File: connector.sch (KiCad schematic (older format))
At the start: 17 parts

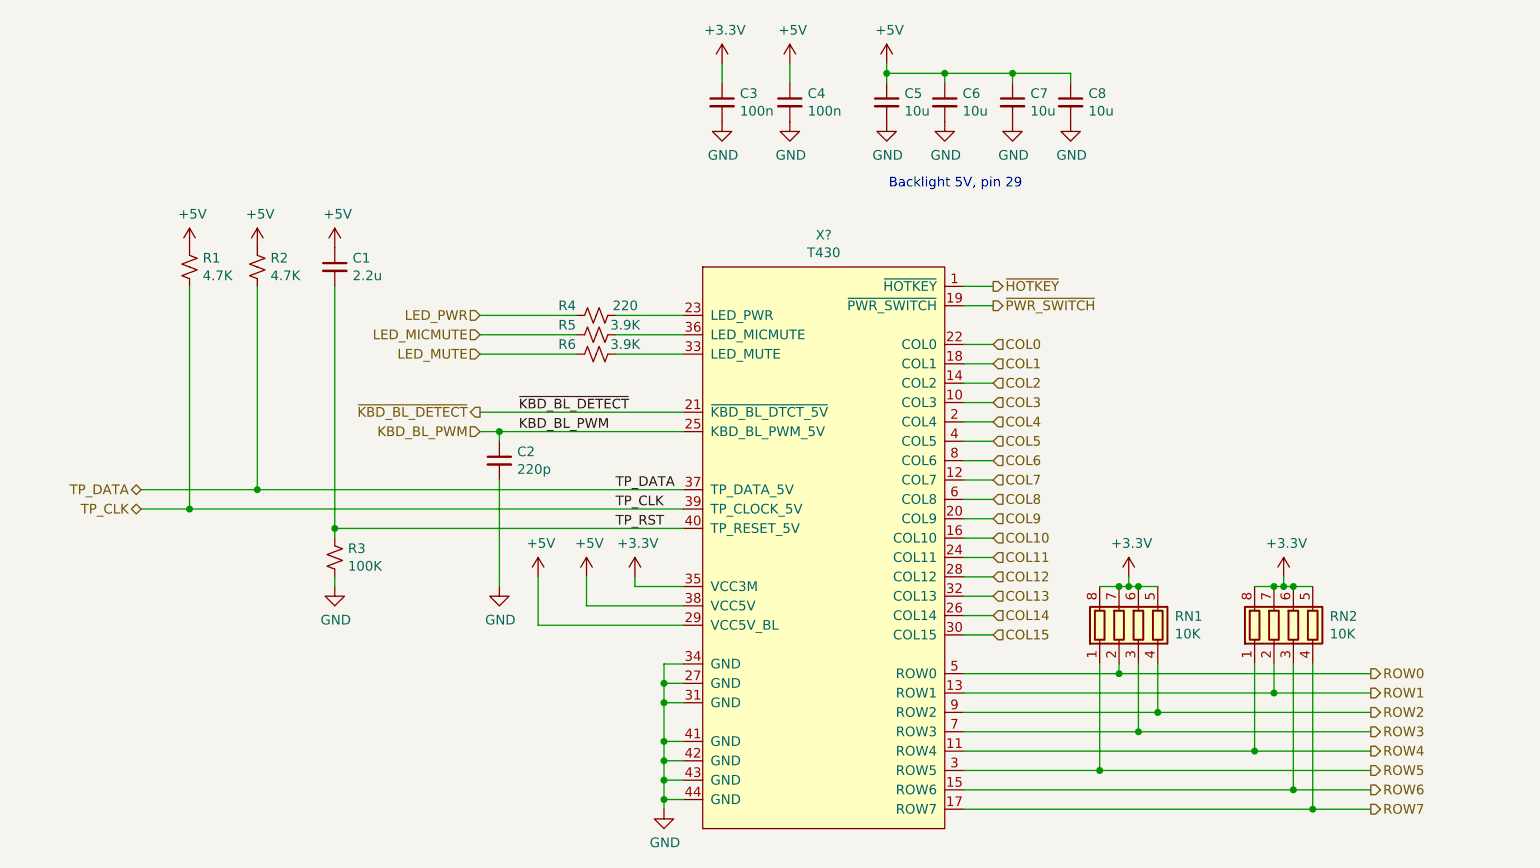
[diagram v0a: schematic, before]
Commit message: Added 'do not populate' for Trackpoint and rows
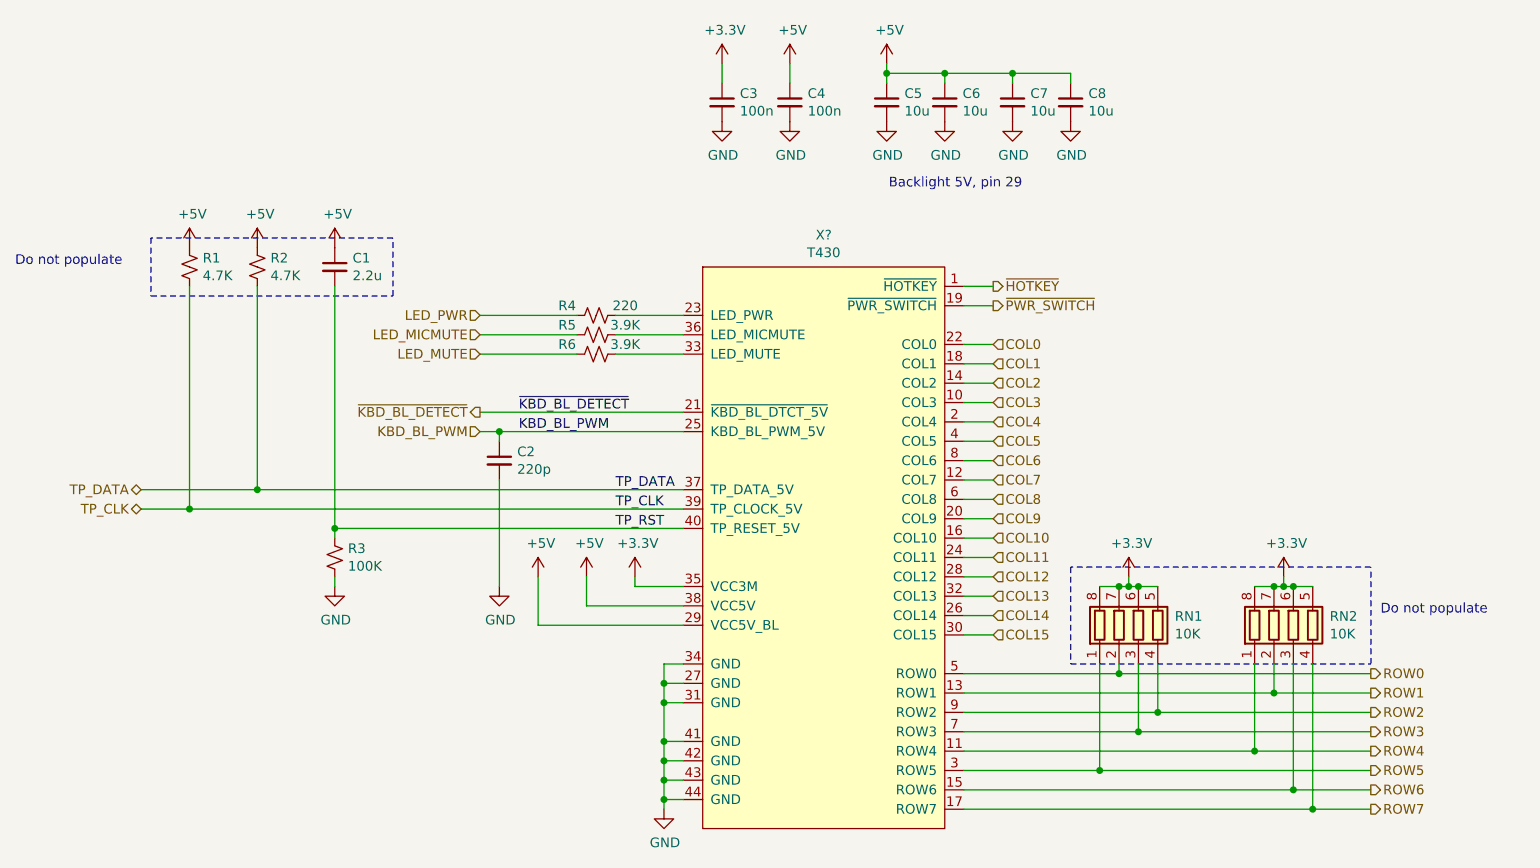
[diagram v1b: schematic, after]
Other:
- note added: "Do not populate"
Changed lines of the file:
@@
 	1    0    0    -1
 $EndComp
+Text Notes 1450 2200 0    50   ~ 0
+Do not populate
+Wire Notes Line
+	2150 2050 2150 2350
+Wire Notes Line
+	2150 2350 3400 2350
+Wire Notes Line
+	3400 2350 3400 2050
+Wire Notes Line
+	3400 2050 2150 2050
+Text Notes 8500 4000 0    50   ~ 0
+Do not populate
+Wire Notes Line
+	6900 4250 8450 4250
+Wire Notes Line
+	8450 4250 8450 3750
+Wire Notes Line
+	8450 3750 6900 3750
+Wire Notes Line
+	6900 3750 6900 4250
 $EndSCHEMATC

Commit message: Added next revisions comments
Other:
- note added: "Next rev: wire to controller"
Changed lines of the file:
@@
 Wire Notes Line
 	6900 3750 6900 4250
+Text Notes 3450 2250 0    50   ~ 0
+Next rev: wire to controller
+Wire Notes Line
+	5800 900  5800 1850
+Wire Notes Line
+	5800 1850 7200 1850
+Wire Notes Line
+	7200 1850 7200 900
+Wire Notes Line
+	7200 900  5800 900
+Wire Notes Line
+	3000 2100 4550 2100
+Wire Notes Line
+	4550 2100 4550 2300
+Wire Notes Line
+	4550 2300 3000 2300
+Wire Notes Line
+	3000 2300 3000 2100
 $EndSCHEMATC

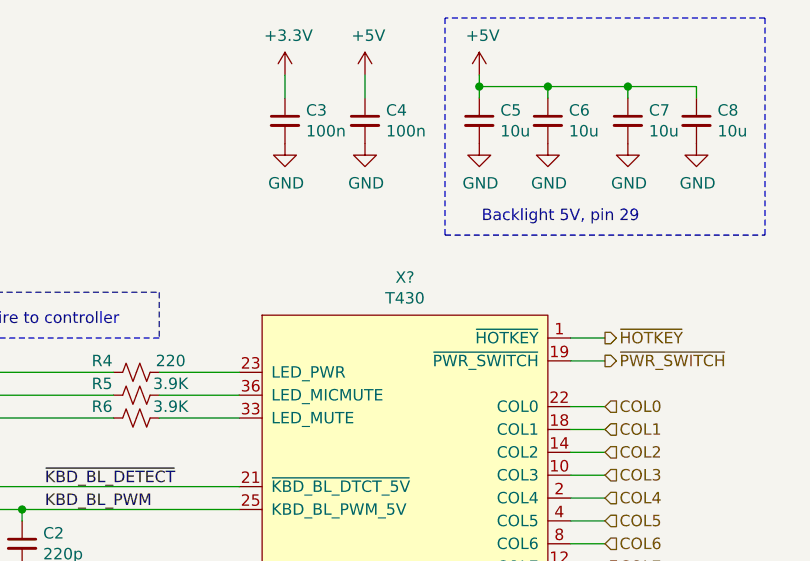
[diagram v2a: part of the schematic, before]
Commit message: Add holes for Teensy
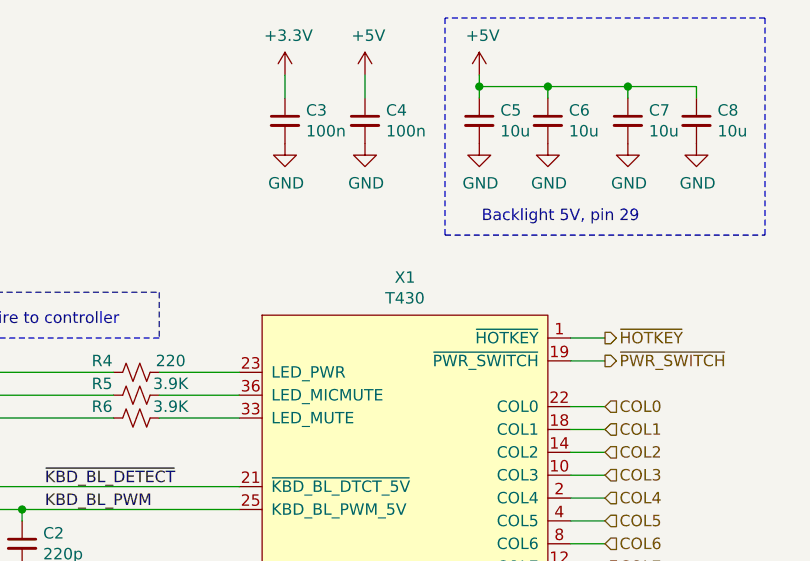
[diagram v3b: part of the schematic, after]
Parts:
- gave numbers to parts that had none: 1
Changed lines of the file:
@@
 EESchema Schematic File Version 4
-LIBS:t430-teensypp-cache
 EELAYER 30 0
 EELAYER END
@@
 $EndComp
 $Comp
-L thinkpad_kbd_connectors:T430 X?
+L thinkpad_kbd_connectors:T430 X1
 U 1 1 5DD7C03F
 P 5000 2200
-F 0 "X?" H 5625 2365 50  0000 C CNN
+F 0 "X1" H 5625 2365 50  0000 C CNN
 F 1 "T430" H 5625 2274 50  0000 C CNN
 F 2 "" H 5900 2200 50  0001 C CNN
